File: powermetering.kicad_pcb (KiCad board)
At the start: 2 copper layers, 194 x 114.1 mm, 211 parts, among them J1 Conn_01x04, J10 CONN_01X02, J2 Conn_01x02, J3 Conn_01x02, J4 Conn_01x02, J5 Conn_01x02, J6 HY951180A_RJ45, J7 CONN_01X02, J8 CONN_01X02, J9 CONN_01X02, P1 USB_OTG, P2 CONN_01X04, U1 KSZ8081, U2 ADE9000, U3 STM32F407VETx, U4 USBLC6-4SC6, U5 ALTAIR04-900, U6 AP1117-50, U7 Si8641ED-B-IS2, U8 NXE2S0505MC, Y1 Crystal, Y2 25M, Y3 RTC

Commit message: finalize proto board and add second board outline
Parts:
- added H1: MountingHole, MountingHole:MountingHole_3.2mm_M3, F.Cu at (59.5, 64.6)
- added H2: MountingHole, MountingHole:MountingHole_3.2mm_M3, F.Cu at (59.5, 155.0)
- added H3: MountingHole, MountingHole:MountingHole_3.2mm_M3, F.Cu at (139.7, 64.6)
- added H4: MountingHole, MountingHole:MountingHole_3.2mm_M3, F.Cu at (139.8, 155.0)
- moved J9 7.06 mm to (260.0, 138.4)
- moved C68 4.32 mm to (251.4, 138.0)
- moved C67 3.00 mm to (246.6, 145.2)
- moved U6 3.00 mm to (252.1, 146.4)
- moved C65 0.85 mm to (255.2, 161.1)
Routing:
- net +5V: track 25.7 -> 22.3 mm
- net Net-(C65-Pad1): track 19.5 -> 20.5 mm
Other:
- board size 194 x 114.1 mm -> 301.6 x 114.1 mm

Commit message: move fuses, add power header
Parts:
- removed H1, H2, H3, H4: MountingHole, MountingHole:MountingHole_3.2mm_M3
- added C58: 100n, stmbl:C_0603, F.Cu at (224.4, 130.6)
- added C81: 1µ, stmbl:C_0805, F.Cu at (216.3, 131.8)
- added C82: 470µ, Capacitor_SMD:CP_Elec_8x10.5, F.Cu at (215.0, 142.5)
- added J11: CONN_01X02, stmbl:Pin_Header_Straight_1x02, F.Cu at (210.9, 130.8)
- added LOGO1: OPEN_HARDWARE_1, stmbl:Symbol_OSHW-Logo_SilkScreen, F.Cu at (146.0, 59.9)
- added REF**: Symbol_HighVoltage_Type2_Top_VerySmall, stmbl:Symbol_HighVoltage_Type2_Top_VerySmall, F.Cu at (135.7, 61.4)
- added RV1: Varistor, Varistor:RV_Disc_D12mm_W3.9mm_P7.5mm, F.Cu at (132.4, 152.8)
- added U10: AP1117-50, Package_TO_SOT_SMD:SOT-223-3_TabPin2, F.Cu at (223.2, 135.7)
- F1, F2, F3, F4: footprint Fuse:Fuseholder_Cylinder-6.3x32mm_Schurter_0031-8002_Horizontal_Open -> Fuse:Fuse_SunFuse-6HP
- moved F4 66.3 mm to (160.0, 88.8)
- moved F3 59.8 mm to (150.0, 88.8)
- moved D21 56.5 mm to (145.0, 134.2)
- moved F2 53.3 mm to (140.0, 88.8)
- moved J9 49.2 mm to (210.9, 134.5), turned to 90 degrees
- moved C18 48.5 mm to (259.2, 112.7)
- moved C20 48.5 mm to (274.2, 112.7)
- moved C75 48.5 mm to (279.6, 131.2)
- moved R40 48.5 mm to (269.5, 88.5)
- moved R56 48.5 mm to (269.8, 149.7)
- moved C1 48.5 mm to (239.6, 131.2)
- moved C10 48.5 mm to (242.7, 124.3)
- moved C11 48.5 mm to (242.7, 121.7)
- moved C12 48.5 mm to (242.7, 119.0)
- moved C14 48.5 mm to (229.2, 112.7)
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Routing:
- net L1: track 88.8 -> 7.22 mm
- net +3V3: track 199.4 -> 264.7 mm, vias 11 -> 12
- net L2: track 73.3 -> 9.96 mm
- net L3: track 42.8 -> 6.61 mm
- net GNDPWR: track 38.7 -> 10.1 mm, vias 27 -> 25
- net Net-(F4-Pad1): track 26.9 -> 0.00 mm
- net Net-(F1-Pad1): track 25.2 -> 0.00 mm
- net Net-(F4-Pad2): track 14.6 -> 0.00 mm
- net Net-(F3-Pad1): track 13.6 -> 0.00 mm
- net Net-(F2-Pad1): track 13.5 -> 0.00 mm
- net +BATT: track 0.00 -> 8.16 mm
- net +5V: track 22.3 -> 27.2 mm
- net MISO: track 29.6 -> 26.9 mm
- net MOSI: track 30.4 -> 27.8 mm
- net SCLK: track 29.8 -> 27.1 mm
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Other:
- board size 301.6 x 114.1 mm -> 194 x 114.1 mm
- board text added: "V1"
- board text added: "https://github.com/sync-/powermetering"

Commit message: V2 hardware
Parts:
- removed C76: 100n, stmbl:C_0805
- removed D10, D11, D12, D13, D14, D15, D16, D17: D, stmbl:SMA_Standard
- removed J10, J11, J8: CONN_01X02, stmbl:Pin_Header_Straight_1x02
- removed LOGO1: OPEN_HARDWARE_1, stmbl:Symbol_OSHW-Logo_SilkScreen
- removed P1: USB_OTG, stmbl:USB_Micro-B
- removed the REF** at (135.7, 61.4)
- added BT1: Battery_Cell, powermetering:18650_keystone_54, F.Cu at (276.5, 103.8)
- added C55: 1µ, stmbl:C_0805, F.Cu at (286.9, 131.6)
- added C80: 100n, stmbl:C_0805, F.Cu at (210.7, 135.3)
- added C83: 100n, stmbl:C_0805, F.Cu at (284.8, 125.7)
- added C84: 100n, stmbl:C_0805, F.Cu at (209.8, 125.5)
- added D25: D, stmbl:SMA_Standard, F.Cu at (213.0, 129.8)
- added D26: D, stmbl:SMA_Standard, F.Cu at (209.7, 132.8)
- added J16: Conn_02x20_Odd_Even, Connector_PinHeader_2.54mm:PinHeader_2x20_P2.54mm_Vertical, F.Cu at (254.8, 111.0)
- added R55: 330, stmbl:R_0805, F.Cu at (283.1, 125.7)
- added R69: 2.7k, stmbl:R_0805, F.Cu at (286.5, 121.1)
- added R70: 1k, stmbl:R_0603, F.Cu at (210.3, 156.6)
- added R71: 1k, stmbl:R_0603, F.Cu at (210.4, 160.6)
- added REF**: Symbol_HighVoltage_Type2_Top_VerySmall, stmbl:Symbol_HighVoltage_Type2_Top_VerySmall, F.Cu at (199.9, 77.0)
- added REF**: Symbol_HighVoltage_Type2_Top_VerySmall, stmbl:Symbol_HighVoltage_Type2_Top_VerySmall, F.Cu at (115.8, 143.0)
- added REF**: OSHW-Logo2_24.3x20mm_SilkScreen, Symbol:OSHW-Logo2_24.3x20mm_SilkScreen, F.Cu at (171.7, 64.2)
- added RV2: Varistor, Varistor:RV_Disc_D12mm_W3.9mm_P7.5mm, F.Cu at (167.3, 87.2)
- added RV3: Varistor, Varistor:RV_Disc_D12mm_W3.9mm_P7.5mm, F.Cu at (167.3, 99.2)
- added RV4: Varistor, Varistor:RV_Disc_D12mm_W3.9mm_P7.5mm, F.Cu at (167.3, 111.2)
- added U11: AP9101CK, Package_TO_SOT_SMD:SOT-23-5, F.Cu at (287.6, 124.7)
- added U12: NFET, stmbl:SOT-23, F.Cu at (291.4, 122.8)
- added U13: NFET, stmbl:SOT-23, F.Cu at (291.4, 126.6)
- added U9: MCP73811T-420I-OT, Package_TO_SOT_SMD:SOT-23-5, F.Cu at (284.1, 131.5)
- D19, D22: footprint stmbl:SMA_Standard -> Diode_SMD:D_SMC
- D2, D3, D4, D5, D6, D7, D8, D9: value D -> D_Schottky_x2_Serial_AKC; footprint stmbl:SMA_Standard -> Package_TO_SOT_SMD:SOT-23
- R34, R35, R36, R37, R38, R39, R40, R41: footprint Resistor_SMD:R_2010_5025Metric -> Resistor_SMD:R_0612_1632Metric
- U7: value Si8641ED-B-IS2 -> Si8641EB-B-IU; footprint Package_SO:SOIC-16W_7.5x10.3mm_P1.27mm -> Package_SO:QSOP-16_3.9x4.9mm_P0.635mm
- Y1: footprint stmbl-kicad-lib:Crystal_SMD_0603_4Pads -> Crystal:Crystal_SMD_3225-4Pin_3.2x2.5mm
- Y2: footprint stmbl:Crystal_SMD_0603_4Pads -> Crystal:Crystal_SMD_3225-4Pin_3.2x2.5mm
- Y3: footprint stmbl:Crystal_SMD_0603_4Pads -> Crystal:Crystal_SMD_3215-2Pin_3.2x1.5mm
- moved R64 67.8 mm to (253.0, 101.7), turned to 90 degrees
- moved R65 66.8 mm to (251.1, 101.7), turned to 90 degrees
- moved U8 66.4 mm to (201.7, 120.8), turned to 180 degrees
- moved R66 65.9 mm to (249.2, 101.7), turned to 90 degrees
- moved R67 65.0 mm to (247.3, 101.7), turned to 90 degrees
- moved D28 62.4 mm to (253.0, 105.9), turned to 270 degrees
- moved D29 61.3 mm to (251.1, 105.9), turned to 270 degrees
- moved C75 61.2 mm to (218.9, 139.4), turned to 180 degrees
- moved D1 60.3 mm to (200.7, 112.4), turned to 180 degrees
- moved D30 60.3 mm to (249.2, 105.9), turned to 270 degrees
- moved D31 59.4 mm to (247.3, 105.9), turned to 270 degrees
- moved R2 56.3 mm to (204.1, 112.4), turned to 0 degrees
- moved C48 55.2 mm to (244.2, 110.7), turned to 225 degrees
- moved C53 54.6 mm to (248.2, 112.7), turned to 270 degrees
- moved Y3 54.2 mm to (243.7, 104.6), turned to 0 degrees
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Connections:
- net Net-(F4-Pad2) renamed GNDS
- net Net-(U3-Pad92) renamed MMDVM_GPIO5
- D2 pad 1: N -> Net-(D2-Pad1)
- D2 pad 2: Net-(D10-Pad1) -> Net-(D2-Pad1)
- D3 pad 1: Net-(D11-Pad2) -> Net-(D3-Pad1)
- D3 pad 2: N -> Net-(D3-Pad1)
- D4 pad 1: N -> Net-(D4-Pad1)
- D4 pad 2: Net-(D12-Pad1) -> Net-(D4-Pad1)
- D5 pad 1: Net-(D13-Pad2) -> Net-(D5-Pad1)
- D5 pad 2: N -> Net-(D5-Pad1)
- D6 pad 1: N -> Net-(D6-Pad1)
- D6 pad 2: Net-(D14-Pad1) -> Net-(D6-Pad1)
- D7 pad 1: Net-(D15-Pad2) -> Net-(D7-Pad1)
- D7 pad 2: N -> Net-(D7-Pad1)
- D8 pad 1: N -> Net-(D8-Pad1)
- D8 pad 2: Net-(D16-Pad1) -> Net-(D8-Pad1)
- D9 pad 1: Net-(D17-Pad2) -> Net-(D9-Pad1)
- D9 pad 2: N -> Net-(D9-Pad1)
- J2 pad 1: Net-(D10-Pad1) -> Net-(D2-Pad1)
- J2 pad 2: Net-(D11-Pad2) -> Net-(D3-Pad1)
- J3 pad 1: Net-(D12-Pad1) -> Net-(D4-Pad1)
- J3 pad 2: Net-(D13-Pad2) -> Net-(D5-Pad1)
- J4 pad 1: Net-(D14-Pad1) -> Net-(D6-Pad1)
- J4 pad 2: Net-(D15-Pad2) -> Net-(D7-Pad1)
- J5 pad 1: Net-(D16-Pad1) -> Net-(D8-Pad1)
- J5 pad 2: Net-(D17-Pad2) -> Net-(D9-Pad1)
- J6 pad 12: Net-(J6-Pad12) -> ETH_LED
- R14 pad 2: Net-(D10-Pad1) -> Net-(D2-Pad1)
- R15 pad 2: Net-(D11-Pad2) -> Net-(D3-Pad1)
- R16 pad 2: Net-(D12-Pad1) -> Net-(D4-Pad1)
- R17 pad 2: Net-(D13-Pad2) -> Net-(D5-Pad1)
- R18 pad 2: Net-(D14-Pad1) -> Net-(D6-Pad1)
- R19 pad 2: Net-(D15-Pad2) -> Net-(D7-Pad1)
- R20 pad 2: Net-(D16-Pad1) -> Net-(D8-Pad1)
- R21 pad 2: Net-(D17-Pad2) -> Net-(D9-Pad1)
- R34 pad 2: Net-(D10-Pad1) -> Net-(D2-Pad1)
- R35 pad 1: Net-(D11-Pad2) -> Net-(D3-Pad1)
- R36 pad 2: Net-(D12-Pad1) -> Net-(D4-Pad1)
- R37 pad 1: Net-(D13-Pad2) -> Net-(D5-Pad1)
- R38 pad 2: Net-(D14-Pad1) -> Net-(D6-Pad1)
- R39 pad 1: Net-(D15-Pad2) -> Net-(D7-Pad1)
- R40 pad 2: Net-(D16-Pad1) -> Net-(D8-Pad1)
- R41 pad 1: Net-(D17-Pad2) -> Net-(D9-Pad1)
- U1 pad 23: /phy_plug/LED1K -> Net-(J6-Pad9)
- U10 pad 3: +BATT -> Net-(C80-Pad1)
- U3 pad 1: Net-(U3-Pad1) -> Net-(D28-Pad2)
- U3 pad 2: Net-(U3-Pad2) -> Net-(D29-Pad2)
- U3 pad 3: Net-(U3-Pad3) -> Net-(D30-Pad2)
- U3 pad 30: Net-(U3-Pad30) -> SCLK
- U3 pad 31: Net-(U3-Pad31) -> MISO
- U3 pad 55: USART3_TX -> Net-(U3-Pad55)
- U3 pad 56: USART3_RX -> Net-(U3-Pad56)
- U3 pad 77: Net-(U3-Pad77) -> MMDVM_NRST
- U3 pad 78: Net-(U3-Pad78) -> USART3_TX
- U3 pad 79: Net-(U3-Pad79) -> USART3_RX
- U3 pad 80: Net-(U3-Pad80) -> MMDVM_BOOT0
- U3 pad 85: Net-(D28-Pad2) -> Net-(U3-Pad85)
- U3 pad 86: Net-(D29-Pad2) -> Net-(U3-Pad86)
- U3 pad 87: Net-(D30-Pad2) -> Net-(U3-Pad87)
- U3 pad 89: SCLK -> Net-(U3-Pad89)
- U3 pad 90: MISO -> Net-(U3-Pad90)
- U3 pad 93: Net-(U3-Pad93) -> MMDVM_GPIO4
- U3 pad 95: Net-(U3-Pad95) -> MMDVM_GPIO3
- U3 pad 96: Net-(U3-Pad96) -> MMDVM_GPIO2
- U3 pad 97: Net-(U3-Pad97) -> MMDVM_GPIO1
- U3 pad 98: Net-(U3-Pad98) -> MMDVM_GPIO0
- U4 pad 4: SWCLK -> SWIO
- U4 pad 6: SWIO -> SWCLK
- U7 pad 12: Net-(U2-Pad40) -> Net-(U2-Pad39)
- U7 pad 13: Net-(U2-Pad39) -> Net-(U2-Pad37)
- U7 pad 14: Net-(U2-Pad37) -> Net-(U2-Pad40)
- Y1 pad 2: Net-(C2-Pad1) -> Net-(Y1-Pad2)
- Y1 pad 3: (no net) -> Net-(C2-Pad1)
- Y2 pad 2: Net-(C44-Pad1) -> Net-(Y2-Pad2)
- Y2 pad 3: (no net) -> Net-(C44-Pad1)
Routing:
- net +BATT: track 8.16 -> 143.6 mm, vias 0 -> 4
- net +5V: track 27.2 -> 162.3 mm, vias 0 -> 3
- net Net-(BT1-Pad2): track 0.00 -> 72.9 mm
- net ETH_LED: track 0.00 -> 62.4 mm, vias 0 -> 1
- net L1: track 7.22 -> 68.5 mm
- net MMDVM_BOOT0: track 0.00 -> 54.1 mm
- net GNDS: track 0.00 -> 53.4 mm
- net +3V3: track 264.7 -> 313.1 mm, vias 12 -> 11
- net L2: track 9.96 -> 58.3 mm
- net /UL1P: track 69.7 -> 23.1 mm
- net Net-(D13-Pad2): track 40.9 -> 0.00 mm
- net Net-(D10-Pad1): track 40.9 -> 0.00 mm
- net Net-(D11-Pad2): track 40.8 -> 0.00 mm
- net Net-(D17-Pad2): track 40.8 -> 0.00 mm
- net Net-(D12-Pad1): track 40.8 -> 0.00 mm
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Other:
- outline, holes or cut-outs redrawn
- board text added: "V2"
- board text removed: "V1"

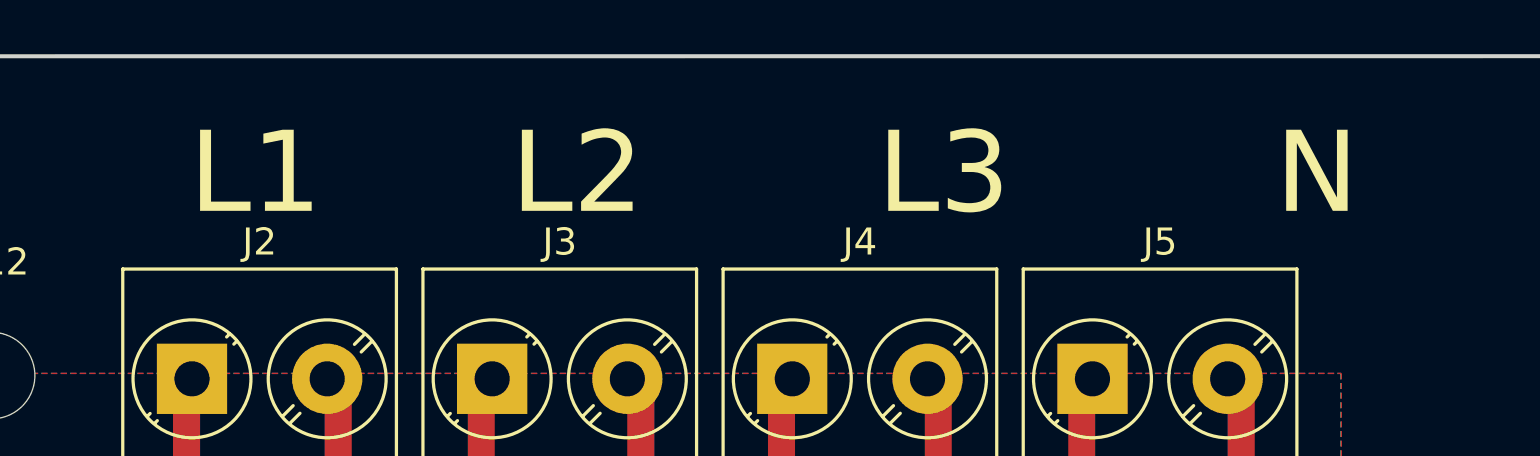
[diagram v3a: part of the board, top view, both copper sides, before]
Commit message: swap phase order on current input
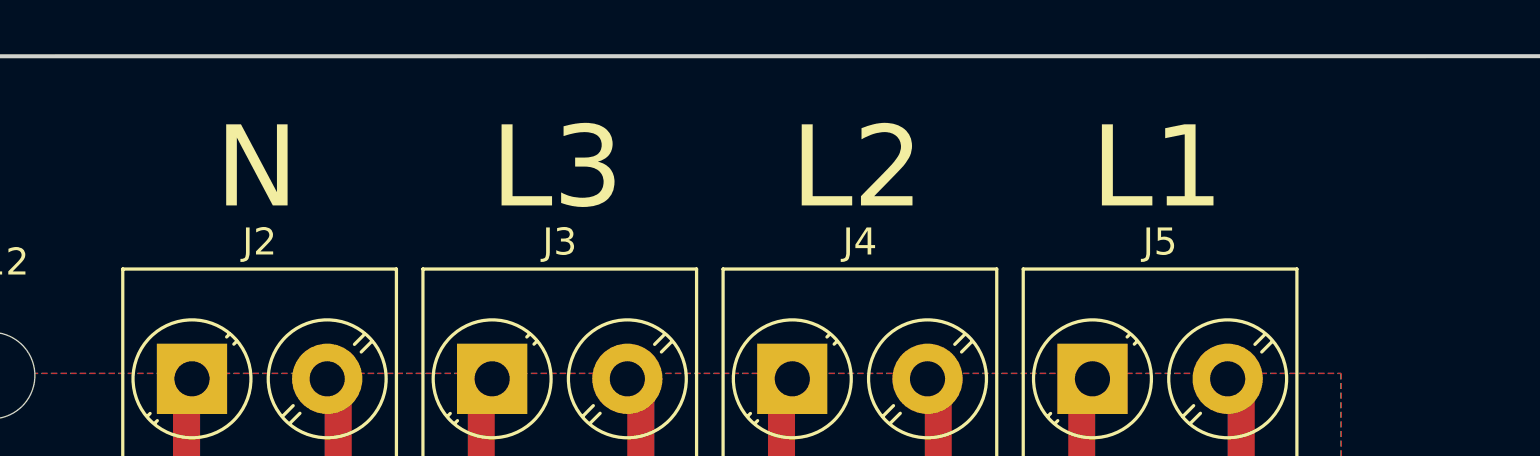
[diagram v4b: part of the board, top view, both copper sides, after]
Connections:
- C13 pad 1: /IL1N -> /INN
- C14 pad 2: /IL1P -> /INP
- C15 pad 1: /IL2N -> /IL3N
- C16 pad 2: /IL2P -> /IL3P
- C17 pad 1: /IL3N -> /IL2N
- C18 pad 2: /IL3P -> /IL2P
- C19 pad 1: /INN -> /IL1N
- C20 pad 2: /INP -> /IL1P
- R10 pad 1: /IL3N -> /IL2N
- R11 pad 1: /IL3P -> /IL2P
- R12 pad 1: /INN -> /IL1N
- R13 pad 1: /INP -> /IL1P
- R6 pad 1: /IL1N -> /INN
- R7 pad 1: /IL1P -> /INP
- R8 pad 1: /IL2N -> /IL3N
- R9 pad 1: /IL2P -> /IL3P
- U2 pad 10: /IL3N -> /IL2N
- U2 pad 11: /IL2P -> /IL3P
- U2 pad 12: /IL2N -> /IL3N
- U2 pad 13: /IL1P -> /INP
- U2 pad 14: /IL1N -> /INN
- U2 pad 7: /INP -> /IL1P
- U2 pad 8: /INN -> /IL1N
- U2 pad 9: /IL3P -> /IL2P
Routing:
- net /INP: track 44.7 -> 14.4 mm
- net /IL1P: track 14.4 -> 44.7 mm
- net /INN: track 40.5 -> 14.1 mm
- net /IL1N: track 14.1 -> 40.5 mm
- net /IL3P: track 32.8 -> 21.8 mm
- net /IL2P: track 21.8 -> 32.8 mm
- net /IL3N: track 27.8 -> 19.4 mm
- net /IL2N: track 19.4 -> 27.8 mm
